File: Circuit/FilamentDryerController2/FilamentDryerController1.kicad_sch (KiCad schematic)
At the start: 37 parts, among them J1 PWR, J2 Fan, J3 I2C, J4 Heat, J5 I2C, J6 100k, Q1 IRL540N or IRFZ20 or IRF740 o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, SW1 Push, U1 ATmega328-P, U2 LM7805_TO220, U3 SN74LVC2G06, Y1 16MHz

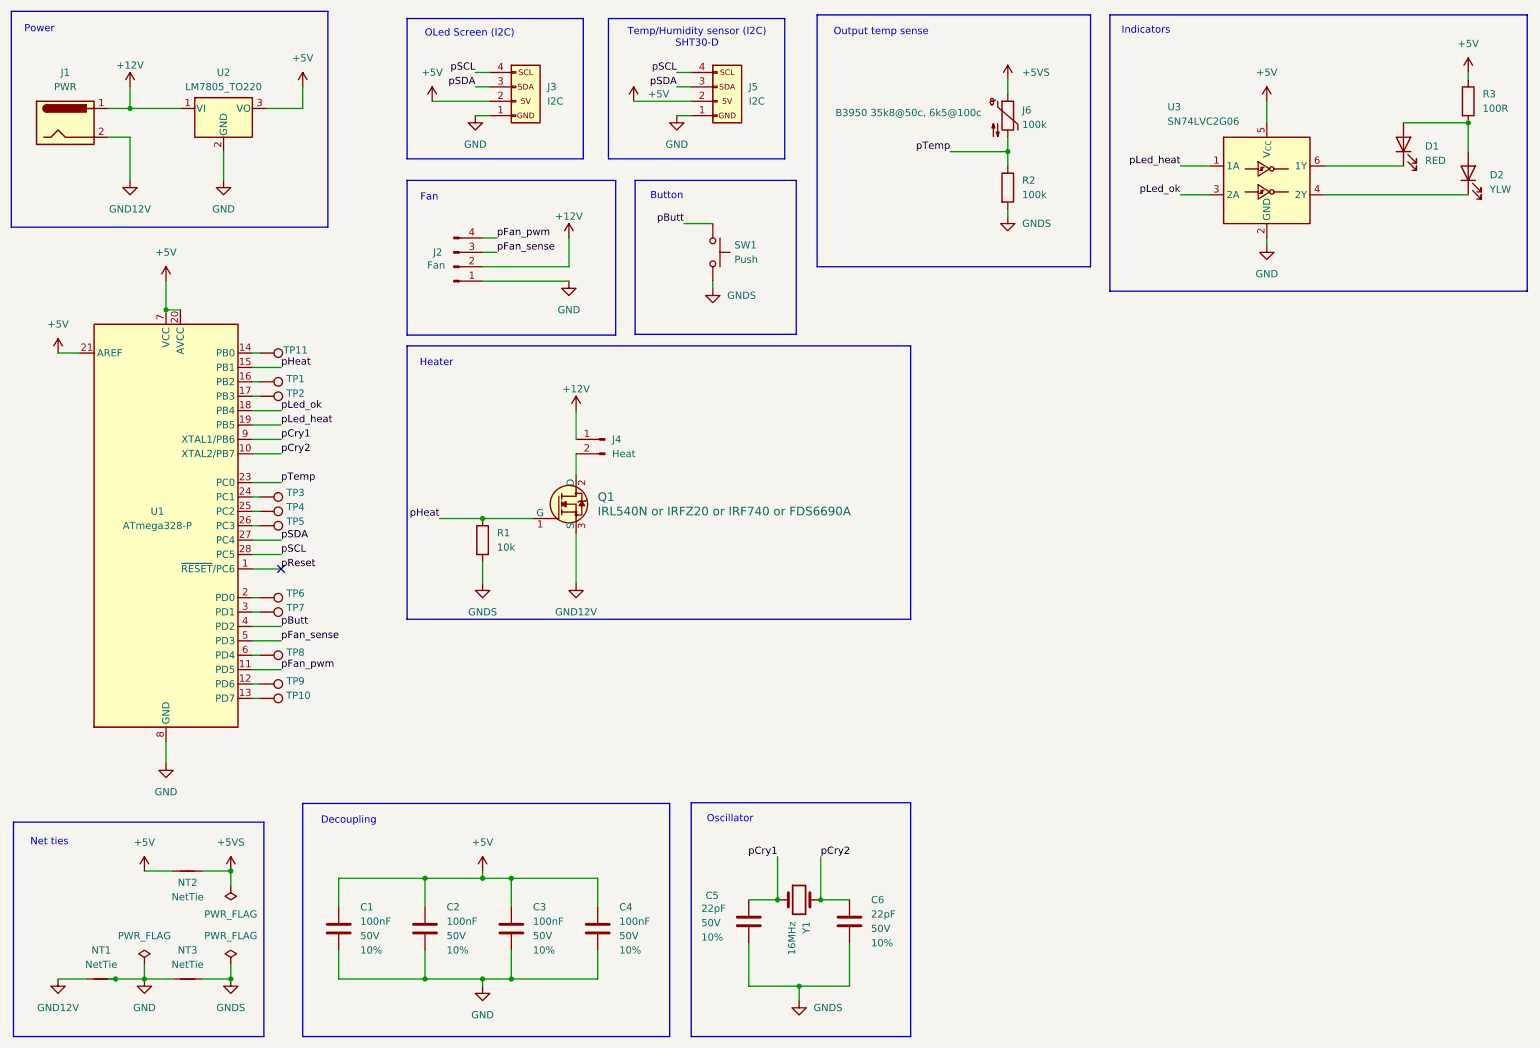
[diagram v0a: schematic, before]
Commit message: Changed heat to AC. Still need to figure out fan.
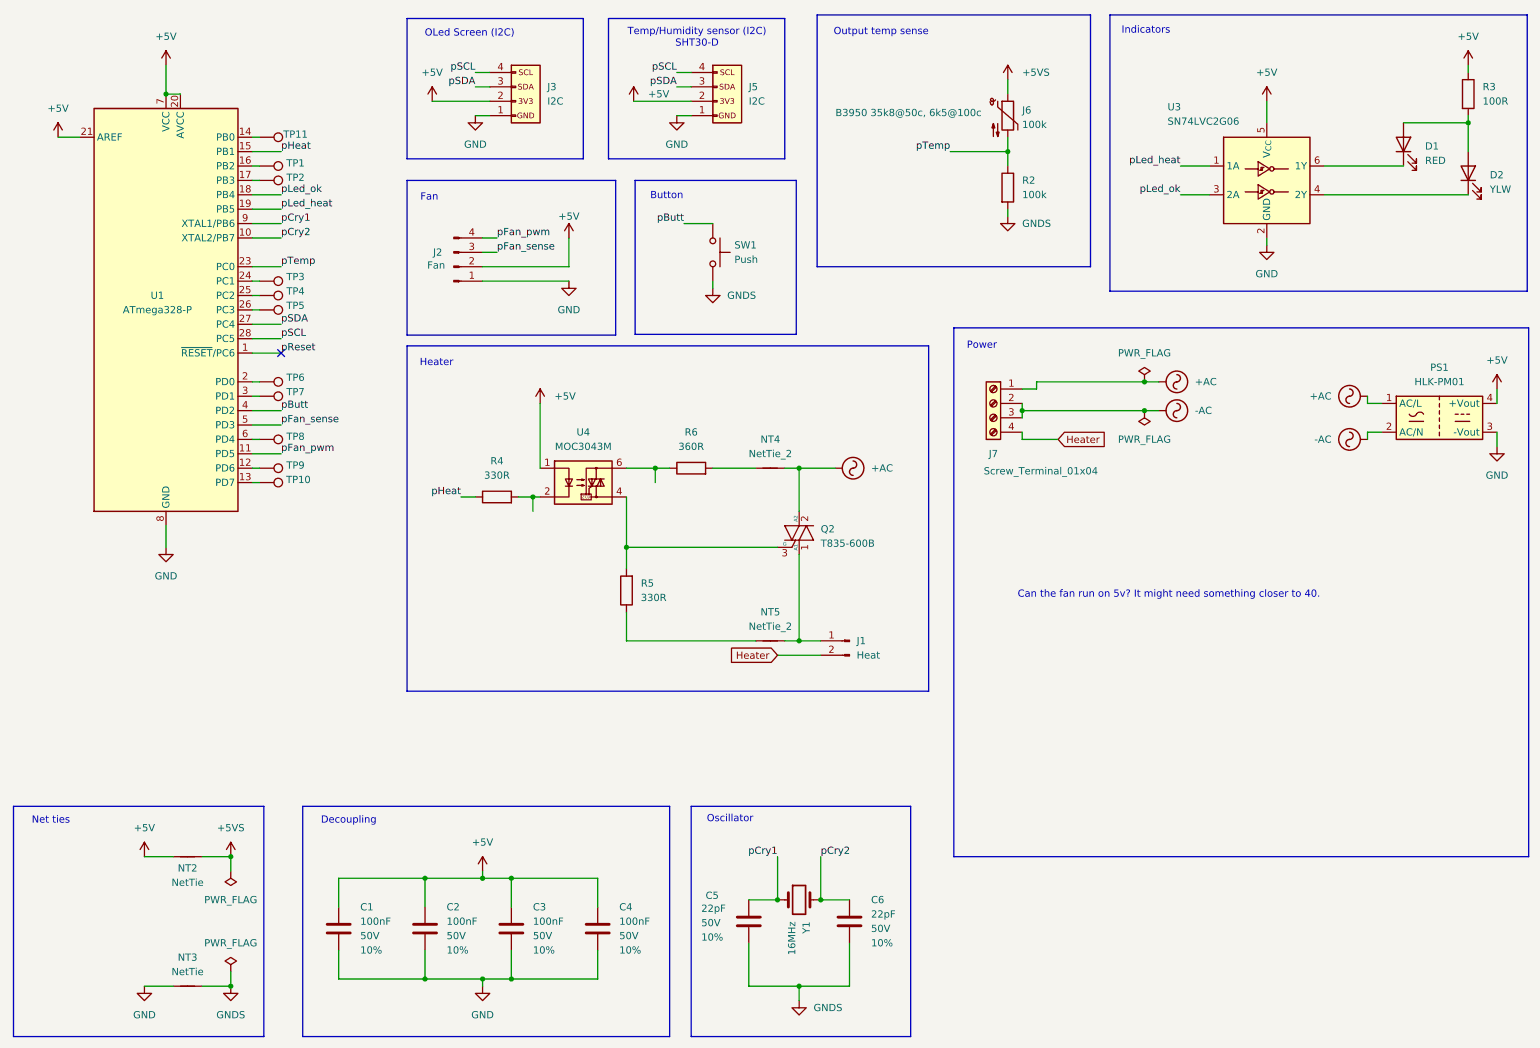
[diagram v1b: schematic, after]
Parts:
- removed J1: PWR, Connector_AMASS:AMASS_XT30U-M_1x02_P5.0mm_Vertical, symbol Connector:Barrel_Jack
- removed J4: Heat, Connector_AMASS:AMASS_XT30UPB-F_1x02_P5.0mm_Vertical, symbol Connector:Conn_01x02_Pin
- removed NT1: NetTie, NetTie:NetTie-2_SMD_Pad2.0mm, symbol Device:NetTie_2
- removed Q1: IRL540N or IRFZ20 or IRF740 or FDS6690A, digikey-footprints:TO-220-3, symbol dk_Transistors-FETs-MOSFETs-Single:IRF540NPBF
- removed R1: 10k, Resistor_SMD:R_1206_3216Metric, symbol Device:R
- removed U2: LM7805_TO220, Package_TO_SOT_THT:TO-220-3_Vertical, symbol Regulator_Linear:LM7805_TO220
- added J1: Heat, Connector_AMASS:AMASS_XT30UPB-F_1x02_P5.0mm_Vertical, symbol Connector:Conn_01x02_Pin
- added J7: Screw_Terminal_01x04, SparkFun-Connector:Screw_Terminal_3.5mm-4, symbol Connector:Screw_Terminal_01x04
- added NT4, NT5: NetTie_2, symbol Device:NetTie_2
- added PS1: HLK-PM01, Converter_ACDC:Converter_ACDC_Hi-Link_HLK-PMxx, symbol Converter_ACDC:HLK-PM01
- added Q2: T835-600B, Package_TO_SOT_SMD:TO-252-2, symbol Triac_Thyristor:BTA16-600B
- added R4, R5: 330R, Resistor_SMD:R_1206_3216Metric, symbol Device:R
- added R6: 360R, Resistor_SMD:R_1206_3216Metric, symbol Device:R
- added U4: MOC3043M, Package_DIP:SMDIP-6_W9.53mm, symbol Relay_SolidState:MOC3043M
- J3, J5: footprint Connector_JST:JST_XH_B4B-XH-A_1x04_P2.50mm_Vertical -> SparkFun-Connector:1x04
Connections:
- net +12V is gone; now on net +5V: J2.2 (Pin_2)
- net +5V: now also PS1.4 (+Vout), U4.1
- net GND: now also PS1.3 (-Vout)
- net pHeat: now also R4.1
- new net: R4.2, U4.2
- new net: Q2.3 (G), R5.2, U4.4
- new net: R6.1, U4.6
- new net: NT4.1, R6.2
- new net: J1.1 (Pin_1), NT5.2, Q2.1 (A1)
- new net: NT5.1, R5.1
- new net +AC: J7.1 (Pin_1), NT4.2, PS1.1 (AC/L), Q2.2 (A2)
- new net -AC: J7.2 (Pin_2), J7.3 (Pin_3), PS1.2 (AC/N)
- new net Heater: J1.2 (Pin_2), J7.4 (Pin_4)
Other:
- note added: "Can the fan run on 5v? It might need something closer to 40."
- moved on the sheet: NT2, NT3, R3, TP1, TP10, TP11, TP2, TP3, TP4, TP5, TP6, TP7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

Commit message: Pcb done.
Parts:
- removed C2, C4: 100nF, SparkFun-Capacitor:C_1206_3216Metric, symbol SparkFun-Capacitor:22uF_1206_50V_10%
- removed J1: Heat, Connector_AMASS:AMASS_XT30UPB-F_1x02_P5.0mm_Vertical, symbol Connector:Conn_01x02_Pin
- removed NT2, NT3: NetTie, NetTie:NetTie-2_SMD_Pad0.5mm, symbol Device:NetTie_2
- added Q1: FDS6690A, Package_SO:SOIC-8_3.9x4.9mm_P1.27mm, symbol Halojen-Symbols:FDS6690A
- added R1: 100k, Resistor_SMD:R_1206_3216Metric, symbol Device:R
- added TP10: PD3, SparkFun-Connector:TestPoint-1.25mm, symbol SparkFun-Connector:TestPoint_PTH
- added TP7: PC6, SparkFun-Connector:TestPoint-1.25mm, symbol SparkFun-Connector:TestPoint_PTH
- C1, C3: footprint SparkFun-Capacitor:C_1206_3216Metric -> Capacitor_SMD:C_1206_3216Metric
- C4: renamed from C5; footprint SparkFun-Capacitor:C_1206_3216Metric -> Capacitor_SMD:C_1206_3216Metric
- C5: renamed from C6; footprint SparkFun-Capacitor:C_1206_3216Metric -> Capacitor_SMD:C_1206_3216Metric
- J1: renamed from J3; footprint SparkFun-Connector:1x04 -> Connector_JST:JST_XH_B4B-XH-A_1x04_P2.50mm_Vertical
- J2: renamed from J5; footprint SparkFun-Connector:1x04 -> Connector_JST:JST_XH_B4B-XH-A_1x04_P2.50mm_Vertical
- J3: renamed from J2; footprint Connector_JST:JST_XH_B4B-XH-A_1x04_P2.50mm_Vertical -> Connector_JST:JST_XH_B2B-XH-A_1x02_P2.50mm_Vertical; symbol Connector:Conn_01x04_Pin -> Connector:Conn_01x02_Pin
- J4: renamed from J6; footprint Connector_JST:JST_XH_B2B-XH-AM_1x02_P2.50mm_Vertical -> Connector_JST:JST_XH_B2B-XH-A_1x02_P2.50mm_Vertical
- NT3: renamed from NT4; value NetTie_2 -> Mains; footprint (none) -> Halojen-Footprints:NetTie-2_SMD_Pad0.2x2.5mm
- NT4: renamed from NT5; value NetTie_2 -> Mains; footprint (none) -> Halojen-Footprints:NetTie-2_SMD_Pad0.2x2.5mm
- SW1: footprint SparkFun-Switch:Push_SMD_6.2x6.2mm -> Button_Switch_SMD:SW_SPST_PTS645
- TP1: renamed from TP11; value PB2 -> PB0; footprint SparkFun-Connector:1x01 -> SparkFun-Connector:TestPoint-1.25mm
- TP11: renamed from TP8; footprint SparkFun-Connector:1x01 -> SparkFun-Connector:TestPoint-1.25mm
- TP12: renamed from TP9; footprint SparkFun-Connector:1x01 -> SparkFun-Connector:TestPoint-1.25mm
- TP13: renamed from TP10; footprint SparkFun-Connector:1x01 -> SparkFun-Connector:TestPoint-1.25mm
- TP2: renamed from TP1; footprint SparkFun-Connector:1x01 -> SparkFun-Connector:TestPoint-1.25mm
- TP3: renamed from TP2; footprint SparkFun-Connector:1x01 -> SparkFun-Connector:TestPoint-1.25mm
- TP4: renamed from TP3; footprint SparkFun-Connector:1x01 -> SparkFun-Connector:TestPoint-1.25mm
- TP5: renamed from TP4; footprint SparkFun-Connector:1x01 -> SparkFun-Connector:TestPoint-1.25mm
- TP6: renamed from TP5; footprint SparkFun-Connector:1x01 -> SparkFun-Connector:TestPoint-1.25mm
- TP8: renamed from TP6; footprint SparkFun-Connector:1x01 -> SparkFun-Connector:TestPoint-1.25mm
- TP9: renamed from TP7; footprint SparkFun-Connector:1x01 -> SparkFun-Connector:TestPoint-1.25mm
- renumbered J7 to J5, R4 to R3, R5 to R4, R6 to R5, R3 to R6, U4 to U2
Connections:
- net +5VS is gone; now on net +5V: J4.1
- net GNDS is gone; now on net GND: C4.2, C5.1, R2.2, SW1.1
- net +5V: now also J3.1 (Pin_1); no longer J3.2 (Pin_2)
- net GND: now also Q1.1 (S), Q1.2 (S), Q1.3 (S), R1.2; no longer J3.1 (Pin_1)
- net Heater: now also NT4.2, Q2.1 (A1)
- net pFan_pwm: now also Q1.4 (G), R1.1; no longer J3.4 (Pin_4)
- net pFan_sense: now also TP10.1; no longer J3.3 (Pin_3)
- net pReset: now also TP7.1
- new net: J3.2 (Pin_2), Q1.5 (D), Q1.6 (D), Q1.7 (D), Q1.8 (D)
- no-connect marks 1 -> 0
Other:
- note removed: "Can the fan run on 5v? It might need something closer to 40."
- moved on the sheet: C1, C3, J5, NT3, NT4, PS1, Q2, R3, R4, R5, SW1, TP1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

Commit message: PCB fabricated.
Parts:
- TP1, TP10, TP11, TP12, TP13, TP2, TP3, TP4, TP5, TP6, TP7, TP8, TP9: now left out of the parts list
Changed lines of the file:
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@@
 	(label "pSDA"
 		(at 96.52 27.94 180)
-		(fields_autoplaced yes)
 		(effects
 			(font
@@
 	(label "pLed_ok"
 		(at 71.12 66.04 0)
-		(fields_autoplaced yes)
 		(effects
 			(font
@@
 	(label "pCry2"
 		(at 157.48 163.83 0)
-		(fields_autoplaced yes)
 		(effects
 			(font
@@
 	(label "pCry2"
 		(at 71.12 73.66 0)
-		(fields_autoplaced yes)
 		(effects
 			(font
@@
 	(label "pFan_sense"
 		(at 77.47 106.68 0)
-		(fields_autoplaced yes)
 		(effects
 			(font
@@
 	(label "pCry1"
 		(at 71.12 71.12 0)
-		(fields_autoplaced yes)
 		(effects
 			(font
@@
 	(label "pTemp"
 		(at 71.12 78.74 0)
-		(fields_autoplaced yes)
 		(effects
 			(font
@@
 	(label "pButt"
 		(at 71.12 104.14 0)
-		(fields_autoplaced yes)
 		(effects
 			(font
@@
 	(label "pSCL"
 		(at 132.08 25.4 180)
-		(fields_autoplaced yes)
 		(effects
 			(font
@@
 	(label "pTemp"
 		(at 180.34 39.37 180)
-		(fields_autoplaced yes)
 		(effects
 			(font
@@
 	(label "pHeat"
 		(at 71.12 58.42 0)
-		(fields_autoplaced yes)
 		(effects
 			(font
@@
 	(label "pSDA"
 		(at 132.08 27.94 180)
-		(fields_autoplaced yes)
 		(effects
 			(font
@@
 	(label "pSCL"
 		(at 71.12 91.44 0)
-		(fields_autoplaced yes)
 		(effects
 			(font
@@
 	(label "pSDA"
 		(at 71.12 88.9 0)
-		(fields_autoplaced yes)
 		(effects
 			(font
@@
 	(label "pLed_heat"
 		(at 71.12 68.58 0)
-		(fields_autoplaced yes)
 		(effects
 			(font
@@
 	(label "pReset"
 		(at 77.47 93.98 0)
-		(fields_autoplaced yes)
 		(effects
 			(font
@@
 	(label "pFan_pwm"
 		(at 71.12 111.76 0)
-		(fields_autoplaced yes)
 		(effects
 			(font
@@
 	(label "pCry1"
 		(at 149.86 163.83 180)
-		(fields_autoplaced yes)
 		(effects
 			(font
@@
 	(label "pButt"
 		(at 132.08 52.07 180)
-		(fields_autoplaced yes)
 		(effects
 			(font
@@
 	(label "pLed_ok"
 		(at 220.98 46.99 180)
-		(fields_autoplaced yes)
 		(effects
 			(font
@@
 	(label "pFan_pwm"
 		(at 139.7 127 180)
-		(fields_autoplaced yes)
 		(effects
 			(font
@@
 	(label "pHeat"
 		(at 201.93 129.54 180)
-		(fields_autoplaced yes)
 		(effects
 			(font
@@
 	(label "pSCL"
 		(at 96.52 25.4 180)
-		(fields_autoplaced yes)
 		(effects
 			(font
@@
 	(label "pLed_heat"
 		(at 220.98 41.91 180)
-		(fields_autoplaced yes)
 		(effects
 			(font
@@
 		(unit 1)
 		(exclude_from_sim no)
-		(in_bom yes)
+		(in_bom no)
 		(on_board yes)
 		(dnp no)
@@
 		(unit 1)
 		(exclude_from_sim no)
-		(in_bom yes)
+		(in_bom no)
 		(on_board yes)
 		(dnp no)
@@
 		(unit 1)
 		(exclude_from_sim no)
-		(in_bom yes)
+		(in_bom no)
 		(on_board yes)
 		(dnp no)
@@
 		(unit 1)
 		(exclude_from_sim no)
-		(in_bom yes)
+		(in_bom no)
 		(on_board yes)
 		(dnp no)
@@
 		(unit 1)
 		(exclude_from_sim no)
-		(in_bom yes)
+		(in_bom no)
 		(on_board yes)
 		(dnp no)
@@
 		(unit 1)
 		(exclude_from_sim no)
-		(in_bom yes)
+		(in_bom no)
 		(on_board yes)
 		(dnp no)
@@
 		(unit 1)
 		(exclude_from_sim no)
-		(in_bom yes)
+		(in_bom no)
 		(on_board yes)
 		(dnp no)
@@
 		(unit 1)
 		(exclude_from_sim no)
-		(in_bom yes)
+		(in_bom no)
 		(on_board yes)
 		(dnp no)
@@
 		(unit 1)
 		(exclude_from_sim no)
-		(in_bom yes)
+		(in_bom no)
 		(on_board yes)
 		(dnp no)
@@
 		(unit 1)
 		(exclude_from_sim no)
-		(in_bom yes)
+		(in_bom no)
 		(on_board yes)
 		(dnp no)
@@
 		(unit 1)
 		(exclude_from_sim no)
-		(in_bom yes)
+		(in_bom no)
 		(on_board yes)
 		(dnp no)
@@
 		(unit 1)
 		(exclude_from_sim no)
-		(in_bom yes)
+		(in_bom no)
 		(on_board yes)
 		(dnp no)
@@
 		(unit 1)
 		(exclude_from_sim no)
-		(in_bom yes)
+		(in_bom no)
 		(on_board yes)
 		(dnp no)
